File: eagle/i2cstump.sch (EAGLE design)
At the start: 20 parts, among them IC1 ATTINY85, IC2 REG1117, Q1 220mA/50V/3.5Ω, Q2 220mA/50V/3.5Ω, X1 USBPCB

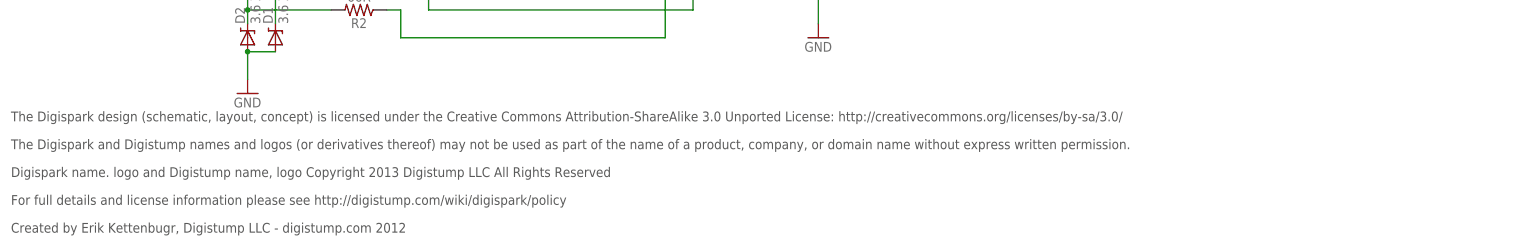
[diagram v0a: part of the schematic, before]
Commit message: Remove text from Digispark -- will attribute in README.md
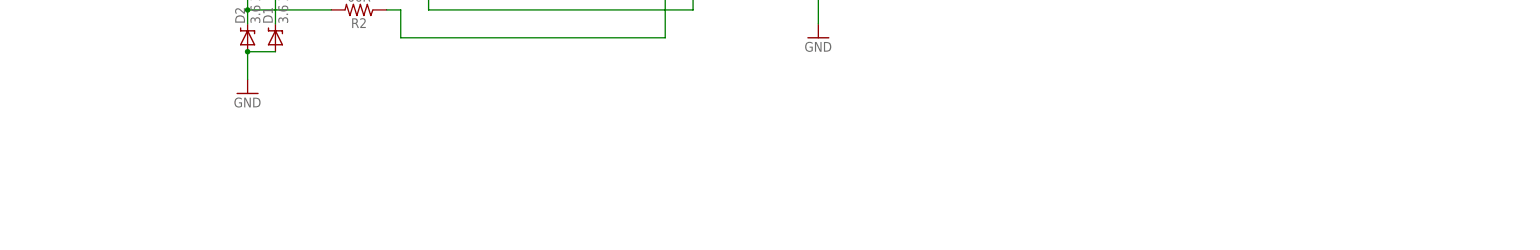
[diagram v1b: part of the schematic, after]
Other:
- note removed: "Created by Erik Kettenbugr, Digistump LLC - digistump.com 2012"
- note removed: "Digispark name. logo and Digistump name, logo Copyright 2013 Digistump LLC All Rights Reserved"
- note removed: "For full details and license information please see http://digistump.com/wiki/digispark/policy"
- note removed: "The Digispark and Digistump names and logos (or derivatives thereof) may not be used as part of the name of a product, company, or domain name without express written permission."
- note removed: "The Digispark design (schematic, layout, concept) is licensed under the Creative Commons Attribution-ShareAlike 3.0 Unported License: http://creativecommons.org/licenses/by-sa/3.0/"
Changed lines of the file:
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@@
 <sheet>
 <plain>
-<text x="-43.18" y="0" size="1.778" layer="97">The Digispark design (schematic, layout, concept) is licensed under the Creative Commons Attribution-ShareAlike 3.0 Unported License: http://creativecommons.org/licenses/by-sa/3.0/</text>
-<text x="-43.18" y="-5.08" size="1.778" layer="97">The Digispark and Digistump names and logos (or derivatives thereof) may not be used as part of the name of a product, company, or domain name without express written permission.</text>
-<text x="-43.18" y="-10.16" size="1.778" layer="97">Digispark name. logo and Digistump name, logo Copyright 2013 Digistump LLC All Rights Reserved</text>
-<text x="-43.18" y="-15.24" size="1.778" layer="97">For full details and license information please see http://digistump.com/wiki/digispark/policy</text>
-<text x="-43.18" y="-20.32" size="1.778" layer="97">Created by Erik Kettenbugr, Digistump LLC - digistump.com 2012</text>
 </plain>
 <instances>

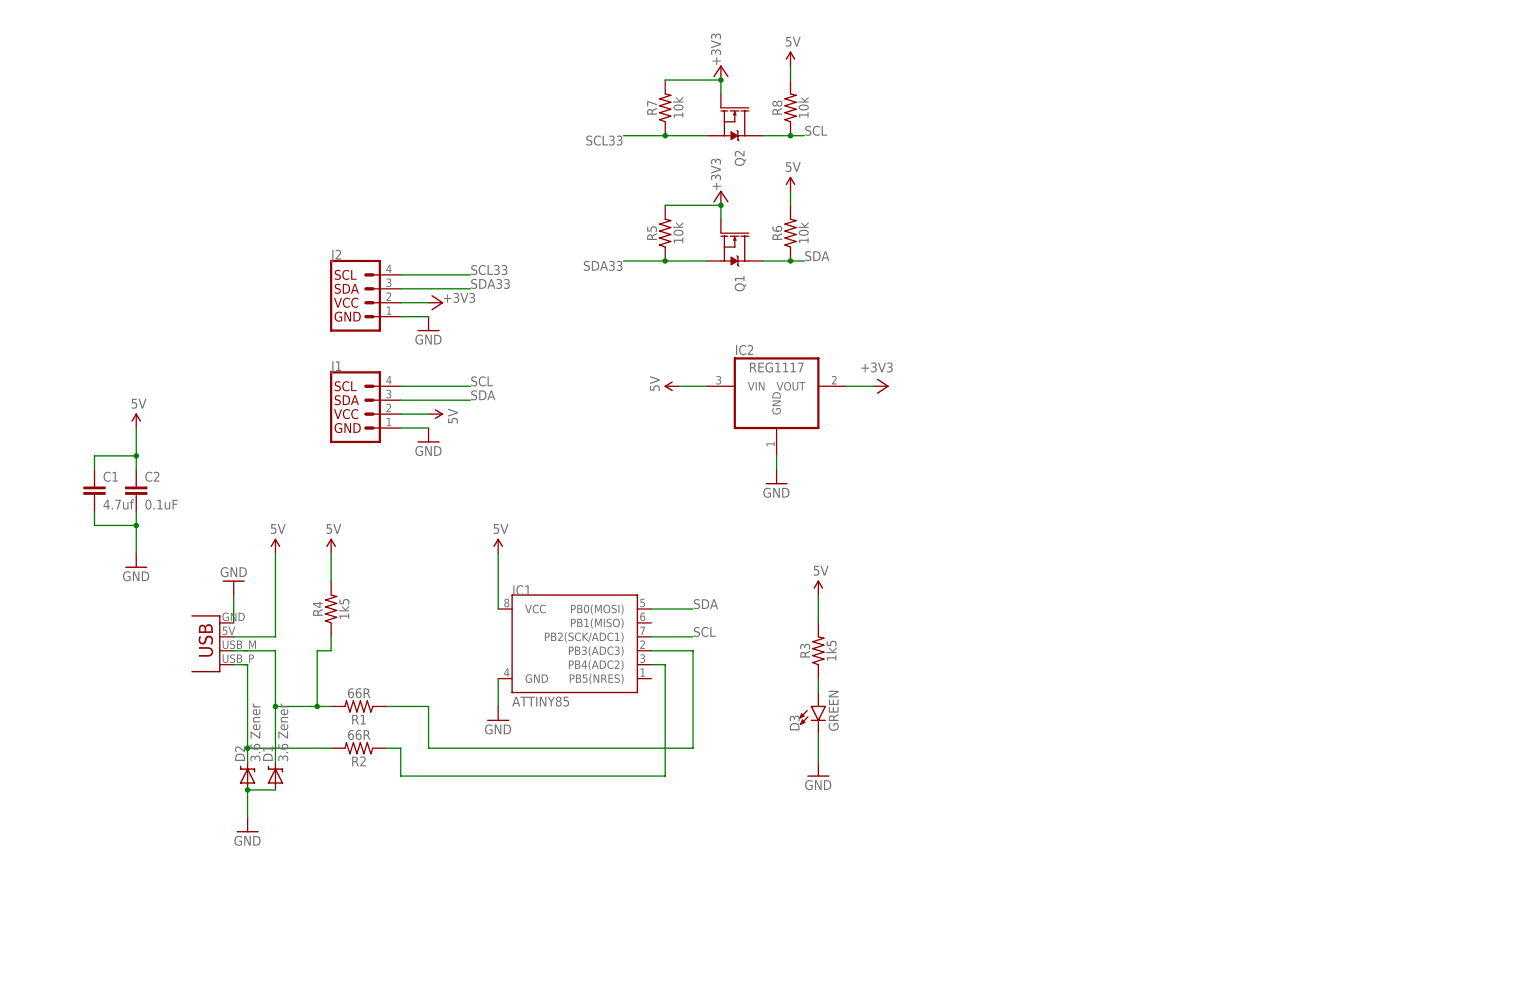
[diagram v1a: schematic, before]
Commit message: Clean up schematic -- split out the levelshifter from the 5V pullups
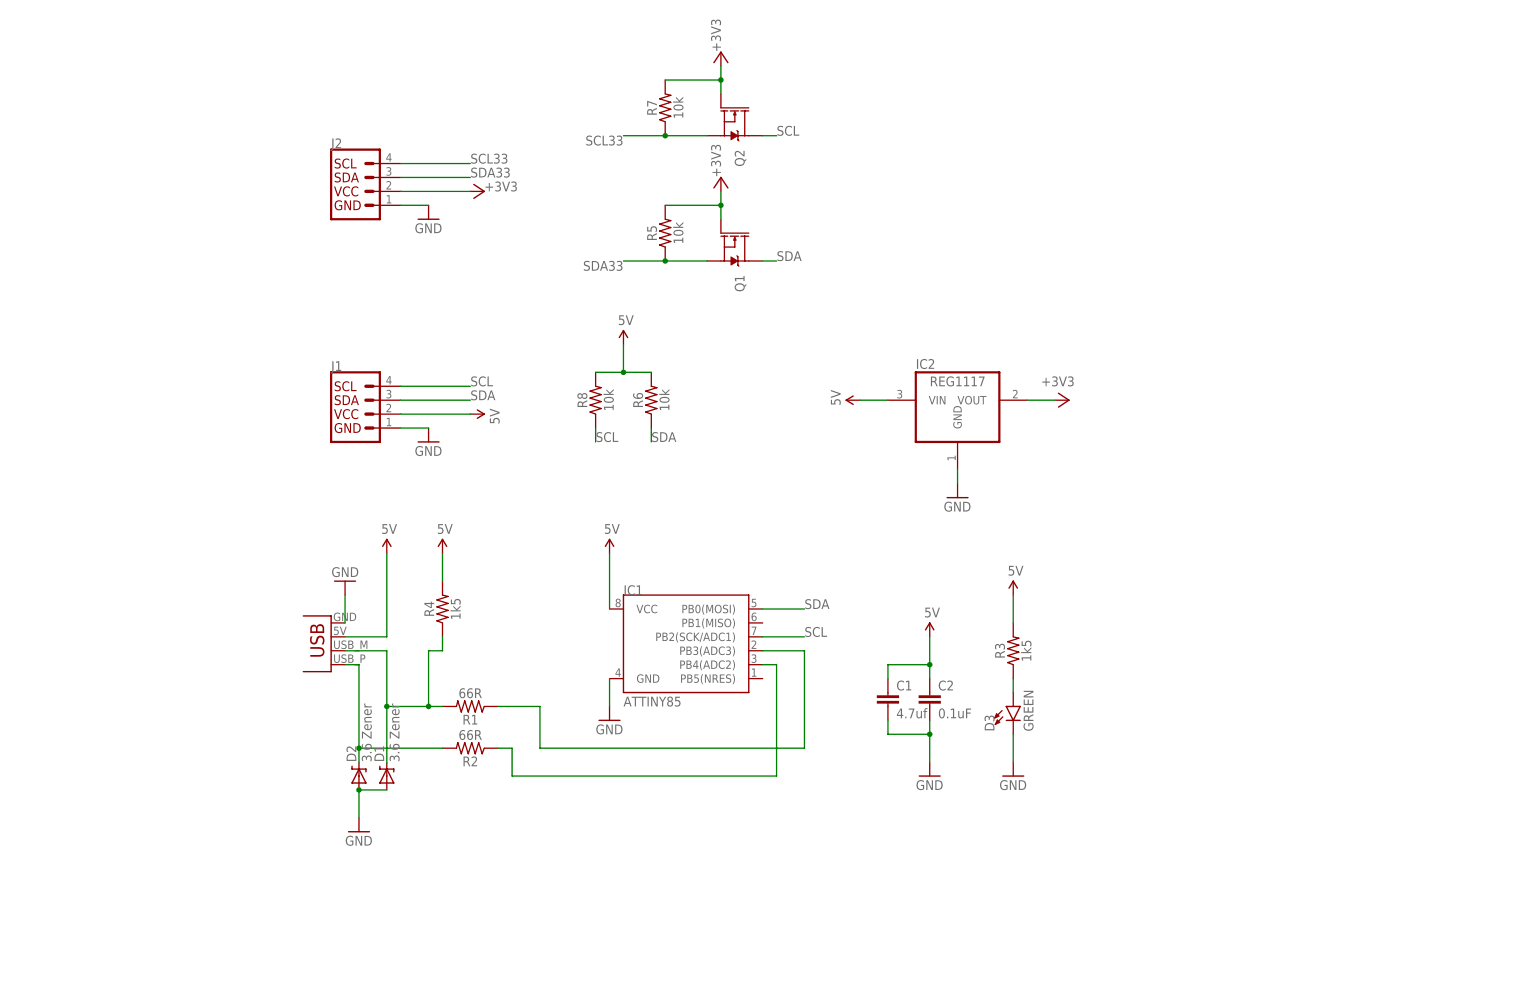
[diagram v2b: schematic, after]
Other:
- moved on the sheet: C1, C2, D1, D2, D3, IC1, IC2, J2, R1, R2, R3, R4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

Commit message: Add some more GND via's - name USB_M and USB_P; Move AM1117 a bit so that 5V has more copper on ingress
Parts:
- added C3: 4.7uf, SparkFun:CAP0805
- J1: value (none) -> I2C-5V
- J2: value (none) -> I2C-3V3
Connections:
- net N$10 renamed USB_M
- net N$11 renamed USB_P
- net +3V3: now also C3.1
- net GND: now also C3.2
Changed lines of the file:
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@@
 <part name="GND13" library="SparkFun" deviceset="GND" device=""/>
 <part name="C1" library="SparkFun" deviceset="CAP" device="0805" value="4.7uf"/>
-<part name="J1" library="SparkFun-Connectors" library_urn="urn:adsk.eagle:library:513" deviceset="QWIIC_CONNECTOR" device="JS-1MM" package3d_urn="urn:adsk.eagle:package:38096/1"/>
+<part name="J1" library="SparkFun-Connectors" library_urn="urn:adsk.eagle:library:513" deviceset="QWIIC_CONNECTOR" device="JS-1MM" package3d_urn="urn:adsk.eagle:package:38096/1" value="I2C-5V"/>
 <part name="U$4" library="SparkFun" deviceset="5V" device=""/>
 <part name="GND4" library="SparkFun" deviceset="GND" device=""/>
@@
 <part name="+3V1" library="supply1" library_urn="urn:adsk.eagle:library:371" deviceset="+3V3" device=""/>
 <part name="GND5" library="SparkFun" deviceset="GND" device=""/>
-<part name="J2" library="SparkFun-Connectors" library_urn="urn:adsk.eagle:library:513" deviceset="QWIIC_CONNECTOR" device="JS-1MM" package3d_urn="urn:adsk.eagle:package:38096/1"/>
+<part name="J2" library="SparkFun-Connectors" library_urn="urn:adsk.eagle:library:513" deviceset="QWIIC_CONNECTOR" device="JS-1MM" package3d_urn="urn:adsk.eagle:package:38096/1" value="I2C-3V3"/>
 <part name="GND6" library="SparkFun" deviceset="GND" device=""/>
 <part name="+3V2" library="supply1" library_urn="urn:adsk.eagle:library:371" deviceset="+3V3" device=""/>
@@
 <part name="U$9" library="SparkFun" deviceset="5V" device=""/>
 <part name="GND8" library="SparkFun" deviceset="GND" device=""/>
+<part name="C3" library="SparkFun" deviceset="CAP" device="0805" value="4.7uf"/>
 </parts>
 <sheets>
@@
 <attribute name="VALUE" x="137.16" y="12.7" size="1.778" layer="96"/>
 </instance>
+<instance part="C3" gate="G$1" x="144.78" y="73.66" smashed="yes">
+<attribute name="NAME" x="146.304" y="76.581" size="1.778" layer="95"/>
+<attribute name="VALUE" x="146.304" y="71.501" size="1.778" layer="96"/>
+</instance>
 </instances>
 <busses>
 </busses>
 <nets>
-<net name="N$10" class="0">
+<net name="USB_M" class="0">
 <segment>
 <pinref part="D1" gate="G$1" pin="C"/>
@@
 </segment>
 </net>
-<net name="N$11" class="0">
+<net name="USB_P" class="0">
 <segment>
 <pinref part="X1" gate="G$1" pin="D+"/>
@@
 <pinref part="GND5" gate="1" pin="GND"/>
 <wire x1="129.54" y1="71.12" x2="129.54" y2="68.58" width="0.1524" layer="91"/>
+<pinref part="C3" gate="G$1" pin="2"/>
+<wire x1="144.78" y1="71.12" x2="129.54" y2="71.12" width="0.1524" layer="91"/>
+<junction x="129.54" y="71.12"/>
 </segment>
 <segment>
@@
 <pinref part="+3V1" gate="G$1" pin="+3V3"/>
 <pinref part="IC2" gate="G$1" pin="VOUT"/>
-<wire x1="147.32" y1="83.82" x2="142.24" y2="83.82" width="0.1524" layer="91"/>
+<wire x1="147.32" y1="83.82" x2="144.78" y2="83.82" width="0.1524" layer="91"/>
+<pinref part="C3" gate="G$1" pin="1"/>
+<wire x1="144.78" y1="83.82" x2="142.24" y2="83.82" width="0.1524" layer="91"/>
+<wire x1="144.78" y1="78.74" x2="144.78" y2="83.82" width="0.1524" layer="91"/>
+<junction x="144.78" y="83.82"/>
 </segment>
 <segment>
@@
 </sheet>
 </sheets>
+<errors>
+</errors>
 </schematic>
 </drawing>
